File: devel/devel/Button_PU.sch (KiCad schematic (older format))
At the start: 3 parts, among them SW1 SW

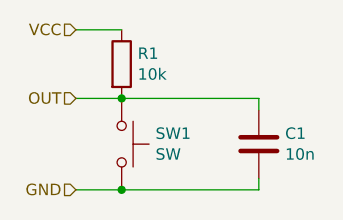
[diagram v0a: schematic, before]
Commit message: Make a physical border
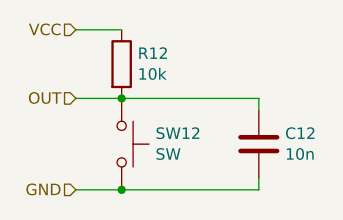
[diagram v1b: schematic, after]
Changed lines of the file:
@@
 EESchema Schematic File Version 4
+LIBS:devel-cache
 EELAYER 26 0
 EELAYER END
@@
 AR Path="/5C594511/5C58179F" Ref="R14"  Part="1"
 AR Path="/5C5956B5/5C58179F" Ref="R23"  Part="1"
-F 0 "R1" H 3470 2296 50  0000 L CNN
+F 0 "R12" H 3470 2296 50  0000 L CNN
 F 1 "10k" H 3470 2205 50  0000 L CNN
 F 2 "Resistor_SMD:R_0805_2012Metric_Pad1.15x1.40mm_HandSolder" V 3330 2250 50  0001 C CNN
@@
 AR Path="/5C594511/5C581B3D" Ref="SW14"  Part="1"
 AR Path="/5C5956B5/5C581B3D" Ref="SW15"  Part="1"
-F 0 "SW1" V 3354 2748 50  0000 L CNN
+F 0 "SW12" V 3354 2748 50  0000 L CNN
 F 1 "SW" V 3445 2748 50  0000 L CNN
 F 2 "Button_Switch_SMD:SW_SPST_EVQQ2" H 3400 2800 50  0001 C CNN
@@
 AR Path="/5C594511/5C581BEA" Ref="C15"  Part="1"
 AR Path="/5C5956B5/5C581BEA" Ref="C16"  Part="1"
-F 0 "C1" H 4115 2646 50  0000 L CNN
+F 0 "C12" H 4115 2646 50  0000 L CNN
 F 1 "10n" H 4115 2555 50  0000 L CNN
 F 2 "Capacitor_SMD:C_0805_2012Metric_Pad1.15x1.40mm_HandSolder" H 4038 2450 50  0001 C CNN

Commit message: Preliminary placement and orientation of components to fit the board
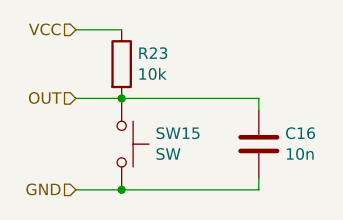
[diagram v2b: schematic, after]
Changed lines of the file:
@@
 $Descr A4 11693 8268
 encoding utf-8
-Sheet 12 18
+Sheet 18 18
 Title ""
 Date ""
@@
 AR Path="/5C594511/5C58179F" Ref="R14"  Part="1"
 AR Path="/5C5956B5/5C58179F" Ref="R23"  Part="1"
-F 0 "R12" H 3470 2296 50  0000 L CNN
+F 0 "R23" H 3470 2296 50  0000 L CNN
 F 1 "10k" H 3470 2205 50  0000 L CNN
 F 2 "Resistor_SMD:R_0805_2012Metric_Pad1.15x1.40mm_HandSolder" V 3330 2250 50  0001 C CNN
@@
 AR Path="/5C594511/5C581B3D" Ref="SW14"  Part="1"
 AR Path="/5C5956B5/5C581B3D" Ref="SW15"  Part="1"
-F 0 "SW12" V 3354 2748 50  0000 L CNN
+F 0 "SW15" V 3354 2748 50  0000 L CNN
 F 1 "SW" V 3445 2748 50  0000 L CNN
 F 2 "Button_Switch_SMD:SW_SPST_EVQQ2" H 3400 2800 50  0001 C CNN
@@
 AR Path="/5C594511/5C581BEA" Ref="C15"  Part="1"
 AR Path="/5C5956B5/5C581BEA" Ref="C16"  Part="1"
-F 0 "C12" H 4115 2646 50  0000 L CNN
+F 0 "C16" H 4115 2646 50  0000 L CNN
 F 1 "10n" H 4115 2555 50  0000 L CNN
 F 2 "Capacitor_SMD:C_0805_2012Metric_Pad1.15x1.40mm_HandSolder" H 4038 2450 50  0001 C CNN
